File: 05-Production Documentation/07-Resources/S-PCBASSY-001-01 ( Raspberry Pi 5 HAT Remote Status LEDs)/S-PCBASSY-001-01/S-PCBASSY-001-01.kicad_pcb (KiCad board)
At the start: 2 copper layers, 65 x 56 mm, 4 parts

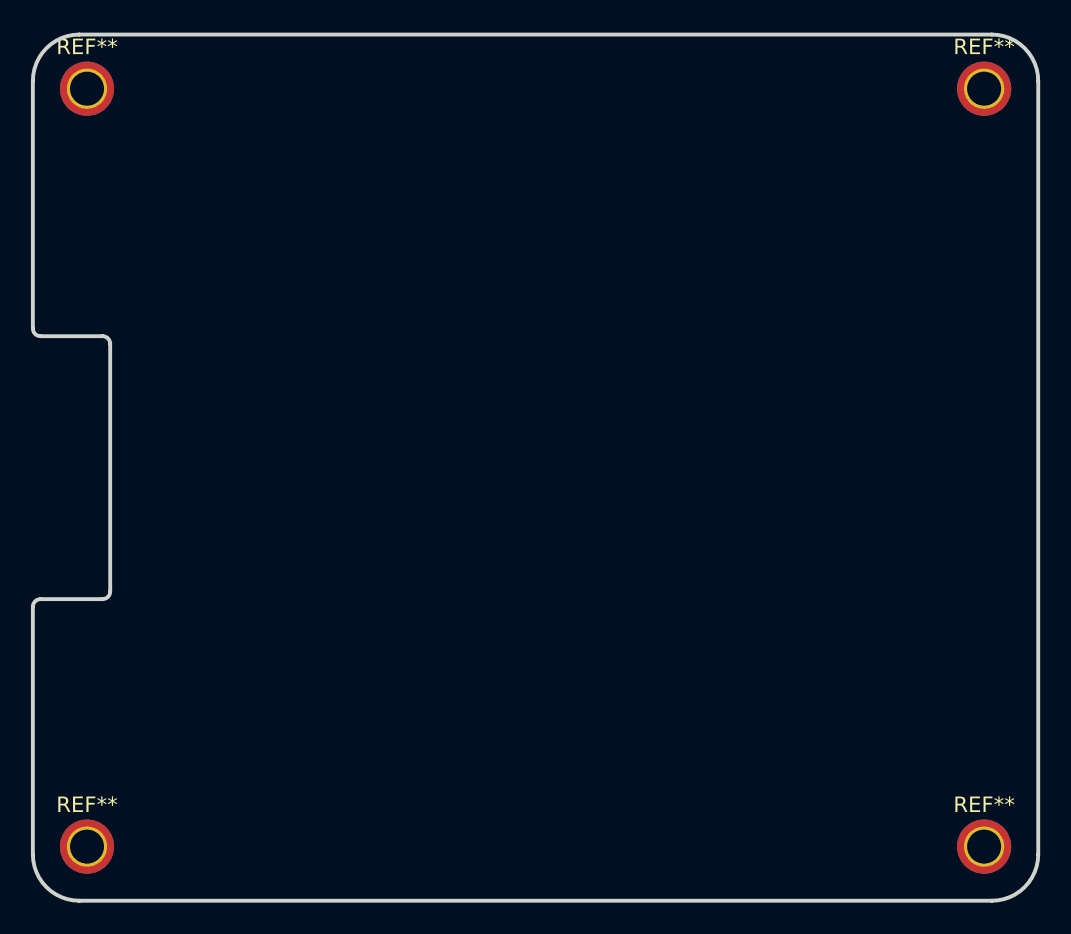
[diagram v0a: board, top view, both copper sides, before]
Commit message: Updated Board Outline
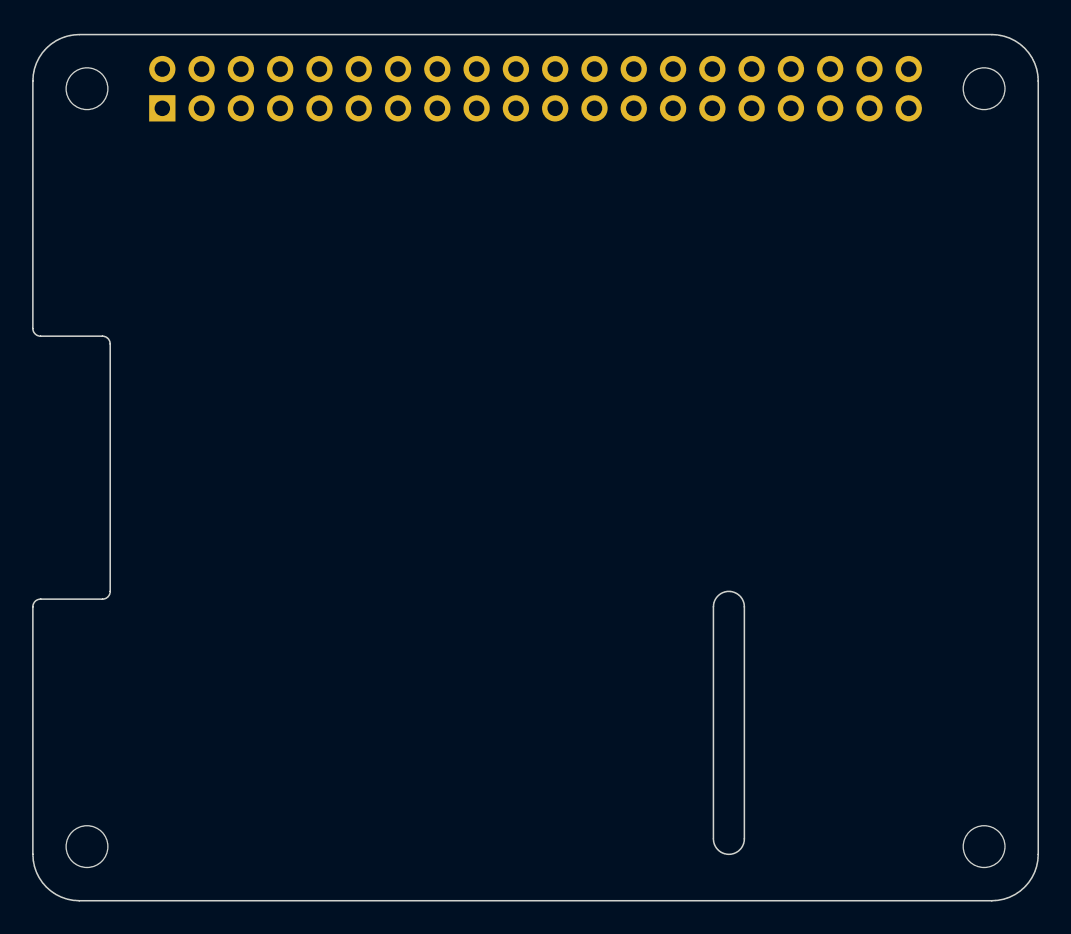
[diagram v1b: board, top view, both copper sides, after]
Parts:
- removed REF** (x4): MountingHole_2.2mm_M2_ISO7380_Pad_TopBottom, MountingHole:MountingHole_2.2mm_M2_ISO7380_Pad_TopBottom
- added J1: GPIO, Connector_PinSocket_2.54mm:PinSocket_2x20_P2.54mm_Vertical, B.Cu at (108.4, 48.8)
- added MH1: MountingHole_2.7mm_M2.5, MountingHole:MountingHole_2.7mm_M2.5, F.Cu at (103.5, 47.5)
- added MH2: MountingHole_2.7mm_M2.5, MountingHole:MountingHole_2.7mm_M2.5, F.Cu at (161.5, 47.5)
- added MH3: MountingHole_2.7mm_M2.5, MountingHole:MountingHole_2.7mm_M2.5, F.Cu at (103.5, 96.5)
- added MH4: MountingHole_2.7mm_M2.5, MountingHole:MountingHole_2.7mm_M2.5, F.Cu at (161.5, 96.5)
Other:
- outline, holes or cut-outs redrawn
- board text added: "CAMERA (OPTIONAL)"
- board text added: "DISPLAY (OPTIONAL)"
- board text added: "Extend PCB edge 0.5mm if using SMT header"
- board text added: "PoE"
- board text added: "RJ45"
- board text added: "USB"

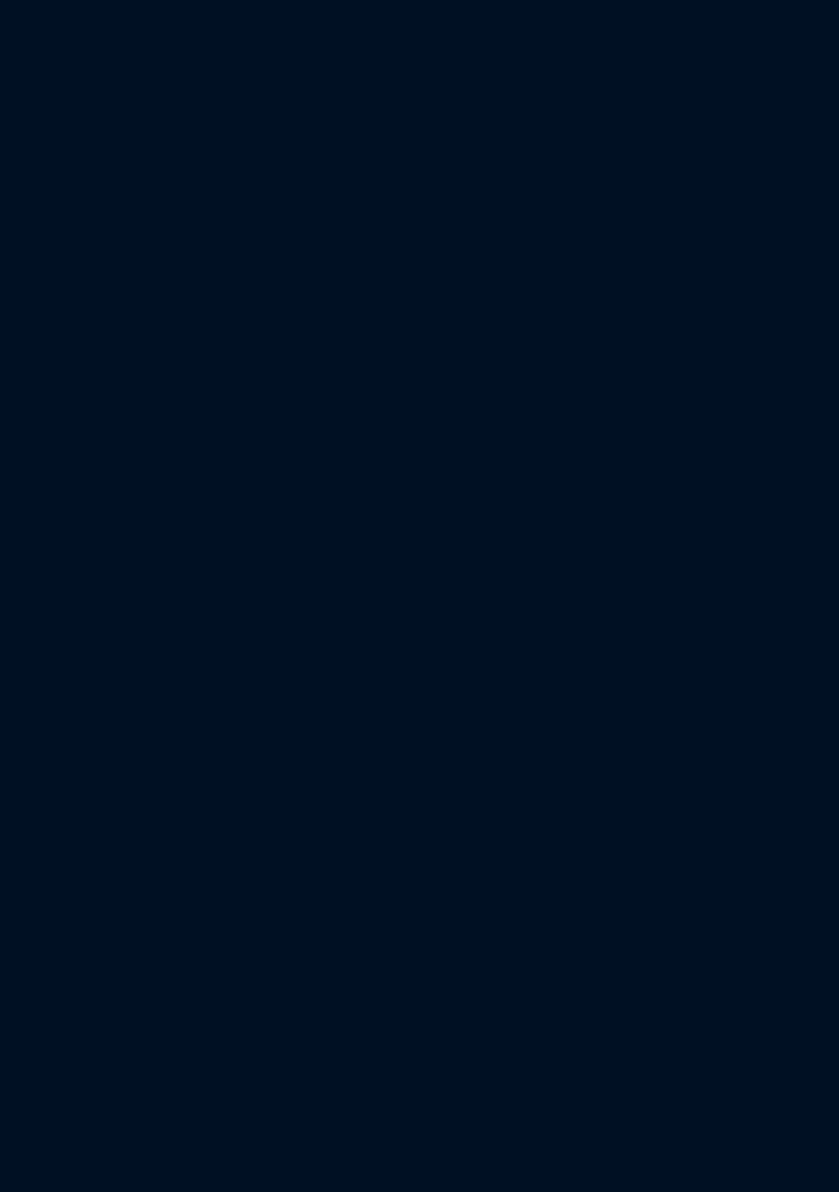
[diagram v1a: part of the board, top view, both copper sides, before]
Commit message: Imported Components to PCB
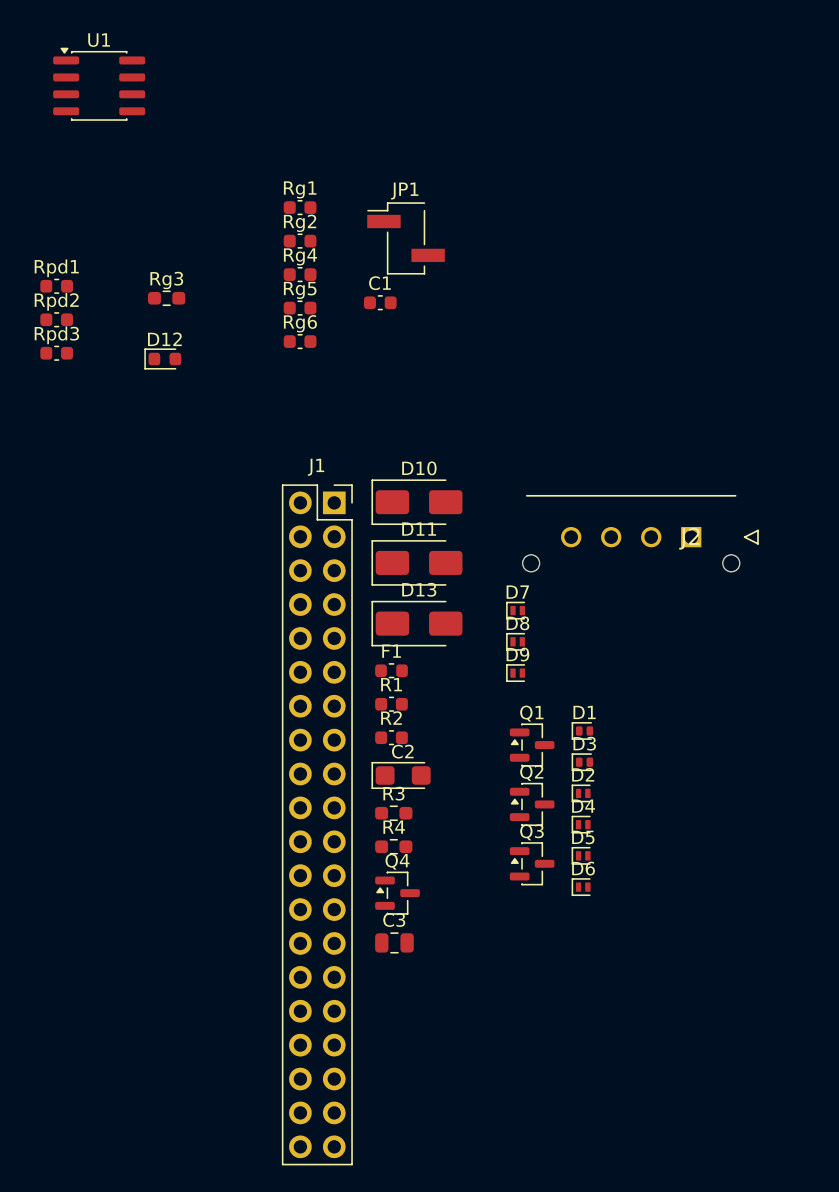
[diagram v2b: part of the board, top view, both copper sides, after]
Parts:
- added C1: 100n, Capacitor_SMD:C_0603_1608Metric, F.Cu at (53.5, 35.6)
- added C2: KEMET T491A106K016AT, Capacitor_Tantalum_SMD:CP_EIA-3216-18_Kemet-A, F.Cu at (55.2, 71.0)
- added C3: Samsung CL21B104KBCNNNC, Capacitor_SMD:C_0805_2012Metric, F.Cu at (54.6, 83.6)
- added D1: PESD5V0L1ULD, Diode_SMD:D_SOD-882D, F.Cu at (68.8, 67.7)
- added D10: 5V6, 3W, Diode_SMD:D_SMA, F.Cu at (56.4, 50.5)
- added D11: 5V6, 3W, Diode_SMD:D_SMA, F.Cu at (56.4, 55.1)
- added D12: LED, LED_SMD:LED_0603_1608Metric, F.Cu at (37.4, 39.8)
- added D13: SS14, Diode_SMD:D_SMA, F.Cu at (56.4, 59.6)
- added D2: PESD5V0S1UL, Diode_SMD:D_SOD-882, F.Cu at (68.7, 72.4)
- added D3: PESD5V0L1ULD, Diode_SMD:D_SOD-882D, F.Cu at (68.8, 70.0)
- added D4: PESD5V0S1UL, Diode_SMD:D_SOD-882, F.Cu at (68.7, 74.7)
- added D5: PESD5V0S1UL, Diode_SMD:D_SOD-882, F.Cu at (68.7, 77.0)
- added D6: PESD5V0S1UL, Diode_SMD:D_SOD-882, F.Cu at (68.7, 79.4)
- added D7: PESD5V0S1UL, Diode_SMD:D_SOD-882, F.Cu at (63.8, 58.7)
- added D8: PESD5V0S1UL, Diode_SMD:D_SOD-882, F.Cu at (63.8, 61.0)
- added D9: PESD5V0S1UL, Diode_SMD:D_SOD-882, F.Cu at (63.8, 63.3)
- added F1: 375mA, Fuse:Fuse_0603_1608Metric, F.Cu at (54.4, 63.2)
- added J1: GPIO, Connector_PinSocket_2.54mm:PinSocket_2x20_P2.54mm_Vertical, F.Cu at (50.1, 50.6)
- added J2: 43650-0428, Connector:43650-04YY_272829, F.Cu at (76.8, 53.1)
- added JP1: ID_WP, Connector_PinHeader_2.54mm:PinHeader_1x02_P2.54mm_Vertical_SMD_Pin1Left, F.Cu at (55.4, 30.8)
- added Q1: BSS138, Package_TO_SOT_SMD:SOT-23, F.Cu at (64.9, 68.7)
- added Q2: BSS138, Package_TO_SOT_SMD:SOT-23, F.Cu at (64.9, 73.2)
- added Q3: BSS138, Package_TO_SOT_SMD:SOT-23, F.Cu at (64.9, 77.6)
- added Q4: AO3401A, Package_TO_SOT_SMD:SOT-23, F.Cu at (54.8, 79.8)
- added R1: 3.9k, Capacitor_SMD:C_0603_1608Metric, F.Cu at (54.4, 65.7)
- added R2: 3.9k, Capacitor_SMD:C_0603_1608Metric, F.Cu at (54.4, 68.2)
- added R3: 2k2, Resistor_SMD:R_0603_1608Metric_Pad0.98x0.95mm_HandSolder, F.Cu at (54.5, 73.8)
- added R4: 100k, Resistor_SMD:R_0603_1608Metric_Pad0.98x0.95mm_HandSolder, F.Cu at (54.5, 76.3)
- added Rg1: 100, Capacitor_SMD:C_0603_1608Metric, F.Cu at (47.5, 28.4)
- added Rg2: 100, Capacitor_SMD:C_0603_1608Metric, F.Cu at (47.5, 31.0)
- added Rg3: 100, Resistor_SMD:R_0603_1608Metric_Pad0.98x0.95mm_HandSolder, F.Cu at (37.5, 35.2)
- added Rg4: 150, Capacitor_SMD:C_0603_1608Metric, F.Cu at (47.5, 33.5)
- added Rg5: 150, Capacitor_SMD:C_0603_1608Metric, F.Cu at (47.5, 36.0)
- added Rg6: 100, Capacitor_SMD:C_0603_1608Metric, F.Cu at (47.5, 38.5)
- added Rpd1: 10k, Capacitor_SMD:C_0603_1608Metric, F.Cu at (29.3, 34.3)
- added Rpd2: 10k, Capacitor_SMD:C_0603_1608Metric, F.Cu at (29.3, 36.9)
- added Rpd3: 10k, Capacitor_SMD:C_0603_1608Metric, F.Cu at (29.3, 39.4)
- added U1: CAT24C256, Package_SO:SOIC-8_3.9x4.9mm_P1.27mm, F.Cu at (32.5, 19.3)
